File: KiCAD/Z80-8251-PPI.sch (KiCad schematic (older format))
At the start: 31 parts, among them J1 SBC8080 BUS, J2 8251-CE, J3 PPI-CE, J4 232C-CON, J5 CON-A, J6 CON-B, J7 OPM-CE, P1 Power, P2 Analog, P3 Digital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

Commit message: REV2 回路図、製造データ出力
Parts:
- removed J2: 8251-CE, Pin_Headers:Pin_Header_Straight_2x08, symbol Z80-8251-PPI-rescue:Conn_02x08_Odd_Even
- removed J3: PPI-CE, Pin_Headers:Pin_Header_Straight_2x08, symbol Z80-8251-PPI-rescue:Conn_02x08_Odd_Even
- removed J7: OPM-CE, Pin_Headers:Pin_Header_Straight_2x08, symbol Z80-8251-PPI-rescue:Conn_02x08_Odd_Even
- removed P1: Power, Socket_Arduino_Uno:Socket_Strip_Arduino_1x08, symbol Z80-8251-PPI-rescue:CONN_01X08
- removed P2: Analog, Socket_Arduino_Uno:Socket_Strip_Arduino_1x06, symbol Z80-8251-PPI-rescue:CONN_01X06
- removed P3: Digital, Socket_Arduino_Uno:Socket_Strip_Arduino_1x10, symbol Z80-8251-PPI-rescue:CONN_01X10
- removed P4: Digital, Socket_Arduino_Uno:Socket_Strip_Arduino_1x08, symbol Z80-8251-PPI-rescue:CONN_01X08
- removed P5, P6, P7, P8: CONN_01X01, Socket_Arduino_Uno:Arduino_1pin, symbol Z80-8251-PPI-rescue:CONN_01X01
- removed R2: 100k, Resistor_THT:R_Axial_DIN0207_L6.3mm_D2.5mm_P10.16mm_Horizontal, symbol Device:R
- removed R3: 1k, Resistor_THT:R_Axial_DIN0207_L6.3mm_D2.5mm_P10.16mm_Horizontal, symbol Device:R
- removed U1: 74HC138, Housings_DIP:DIP-16_W7.62mm_Socket, symbol Z80-8251-PPI-rescue:74LS138
- added C8, C9: 0.1u, Capacitor_THT:C_Rect_L4.0mm_W2.5mm_P2.50mm, symbol Z80-8251-PPI-rescue:C
- added J2: ADDR_JP, Connector_PinHeader_2.54mm:PinHeader_2x04_P2.54mm_Vertical, symbol Connector_Generic:Conn_02x04_Odd_Even
- added J3: IR JP, Connector_PinHeader_2.54mm:PinHeader_1x05_P2.54mm_Horizontal, symbol Connector_Generic:Conn_01x05
- added J7: SERIAL JP, Connector_PinHeader_2.54mm:PinHeader_2x04_P2.54mm_Vertical, symbol Connector_Generic:Conn_02x04_Odd_Even
- added J8: SP JP, Connector_PinHeader_2.54mm:PinHeader_1x02_P2.54mm_Horizontal, symbol Connector_Generic:Conn_01x02
- added JP1: A7_JP, Connector_PinHeader_2.54mm:PinHeader_1x03_P2.54mm_Vertical, symbol Jumper:Jumper_3_Open
- added JP2: VCC_JP, Connector_PinHeader_2.54mm:PinHeader_1x03_P2.54mm_Vertical, symbol Jumper:Jumper_3_Open
- added MH1, MH2, MH3, MH4: MountingHole, MountingHole:MountingHole_3.2mm_M3, symbol Mechanical:MountingHole
- added R2, R4, R5, R6: 100k, Resistor_THT:R_Axial_DIN0207_L6.3mm_D2.5mm_P10.16mm_Horizontal, symbol Device:R_US
- added R3: 1k, Resistor_THT:R_Axial_DIN0207_L6.3mm_D2.5mm_P10.16mm_Horizontal, symbol Device:R_US
- added U1: 74LS139, Package_DIP:DIP-16_W7.62mm_Socket, symbol 74xx:74LS139
- added U5: 8259, Package_DIP:DIP-28_W15.24mm_Socket, symbol Interface:8259
- added U6: 8254, Package_DIP:DIP-24_W15.24mm_Socket, symbol Timer:8254
- C1, C2, C3, C4, C5, C6: footprint Capacitors_THT:C_Rect_L4.0mm_W2.5mm_P2.50mm -> Capacitor_THT:C_Rect_L4.0mm_W2.5mm_P2.50mm
- J4: footprint Pin_Headers:Pin_Header_Angled_1x06 -> Connector_PinHeader_2.54mm:PinHeader_1x06_P2.54mm_Horizontal
- J5, J6: footprint Pin_Headers:Pin_Header_Straight_2x07_Pitch2.54mm -> Connector_PinHeader_2.54mm:PinHeader_2x07_P2.54mm_Vertical
- R1: footprint Resistors_THT:R_Axial_DIN0207_L6.3mm_D2.5mm_P10.16mm_Horizontal -> Resistor_THT:R_Axial_DIN0207_L6.3mm_D2.5mm_P10.16mm_Horizontal
- U2: footprint Housings_DIP:DIP-28_W15.24mm_Socket -> Package_DIP:DIP-28_W15.24mm_Socket
- U3: footprint Housings_DIP:DIP-40_W15.24mm -> Package_DIP:DIP-40_W15.24mm_Socket
- Y1: value 4.9152MHz -> 19.6608MHz
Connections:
- net labels added: 8251-A, 8251A-CS, 8254-1, 8254-2, 8254-CS, 8255-CS, 8259-CS, IR, IR0, IR1, IR2, IR3, IR6, SBC5V, ~INTA
- net labels removed: A2, ~CE, ~RESIN
- wire segments 383 -> 332
- no-connect marks 43 -> 28
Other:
- note added: "+5V"
- note added: "1228.8kHz"
- note added: "153.6kHz"
- note added: "307.2kHz"
- note added: "614.4kHz"
- note added: "CTS"
- note added: "GND"
- note added: "RTS"
- note added: "RxD"
- note added: "TxD"
- note removed: "1"
- note removed: "Holes"
- note removed: "Shield for Arduino that uses\nthe same pin disposition\nlike "Uno" board Rev 3."
- moved on the sheet: C1, C2, C3, C4, C5, C6, C7, J1, J5, J6, R1, U4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

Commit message: REV3 回路図、パターン検討 その1
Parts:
- removed JP2: VCC_JP, Connector_PinHeader_2.54mm:PinHeader_1x03_P2.54mm_Vertical, symbol Jumper:Jumper_3_Open
- added C10: 22p, Capacitor_THT:C_Disc_D3.0mm_W1.6mm_P2.50mm, symbol Device:C_Small
- added JP2: USB POWER, Jumper:SolderJumper-2_P1.3mm_Open_RoundedPad1.0x1.5mm, symbol Jumper:SolderJumper_2_Open
- added JP3: G0 JP, Jumper:SolderJumper-2_P1.3mm_Open_RoundedPad1.0x1.5mm, symbol Jumper:SolderJumper_2_Open
- added JP4: G1 JP, Jumper:SolderJumper-2_P1.3mm_Open_RoundedPad1.0x1.5mm, symbol Jumper:SolderJumper_2_Open
- added JP5: G2 JP, Jumper:SolderJumper-2_P1.3mm_Open_RoundedPad1.0x1.5mm, symbol Jumper:SolderJumper_2_Open
- added JP6, JP7: 8254-1JP, Jumper:SolderJumper-3_P1.3mm_Bridged12_RoundedPad1.0x1.5mm, symbol Jumper:SolderJumper_3_Bridged12
- C1, C2, C3, C4, C5, C6, C8, C9: footprint Capacitor_THT:C_Rect_L4.0mm_W2.5mm_P2.50mm -> Capacitor_THT:C_Disc_D3.0mm_W1.6mm_P2.50mm
- U5: symbol Interface:8259 -> Z80-8251-PPI-rescue:8259-Interface
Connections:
- net labels added: G0, G1, G2
- net labels removed: SBC5V
- wire segments 332 -> 359
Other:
- moved on the sheet: J8, R2

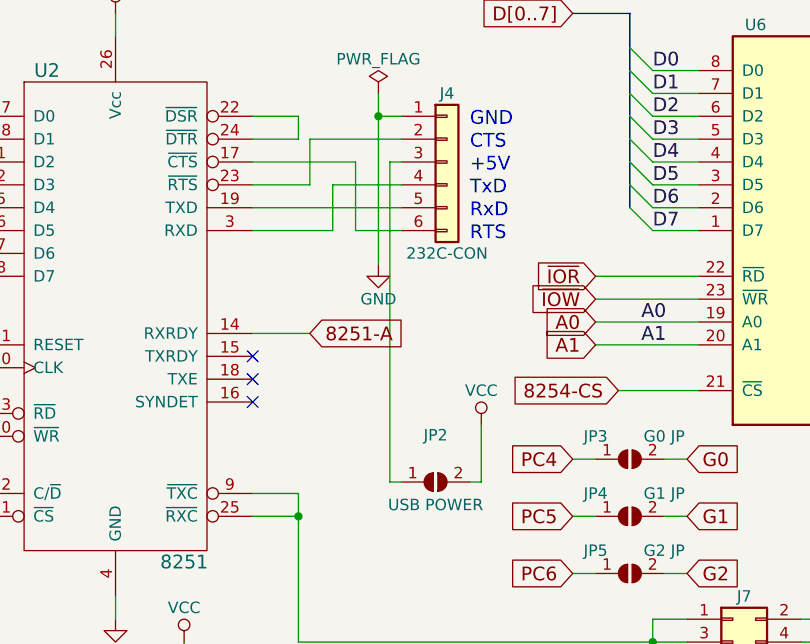
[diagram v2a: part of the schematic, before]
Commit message: FTDI +5Vへダイオード追加
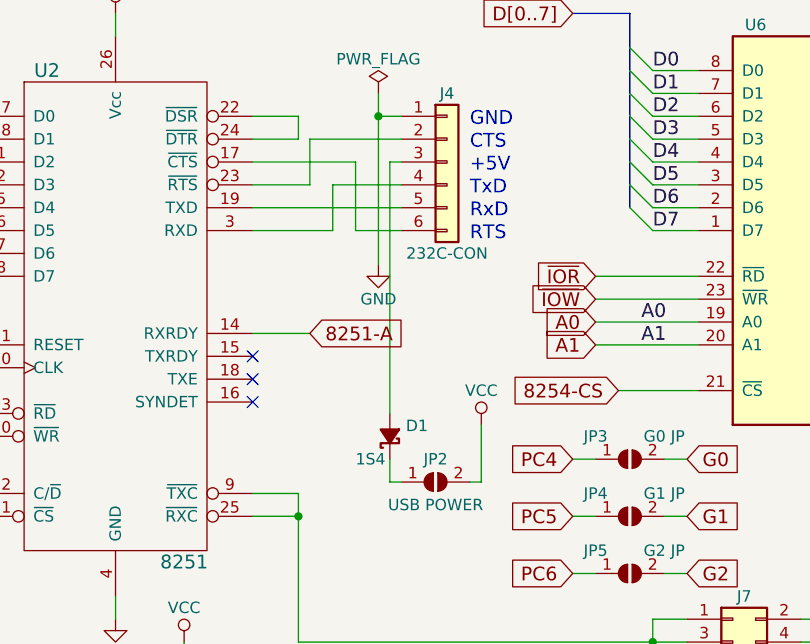
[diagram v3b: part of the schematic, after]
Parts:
- added D1: 1S4, Diode_THT:D_DO-34_SOD68_P7.62mm_Horizontal, symbol Device:D_Schottky_Small_ALT
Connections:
- net at J4.3 (Pin_3): now also D1.2 (A); no longer JP2.1 (A)
- new net: D1.1 (K), JP2.1 (A)
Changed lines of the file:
@@
 Wire Wire Line
 	6700 1450 6650 1450
-Wire Wire Line
-	6650 1450 6650 2850
 $Comp
 L Z80-8251-PPI-rescue:C C8
@@
 U 1 1 5F58D8D7
 P 6850 2850
-F 0 "JP2" H 6850 3055 50  0000 C CNN
+F 0 "JP2" H 6850 2950 50  0000 C CNN
 F 1 "USB POWER" H 6850 2750 50  0000 C CNN
 F 2 "Jumper:SolderJumper-2_P1.3mm_Open_RoundedPad1.0x1.5mm" H 6850 2850 50  0001 C CNN
@@
 Wire Wire Line
 	10200 1850 9200 1850
+$Comp
+L Device:D_Schottky_Small_ALT D1
+U 1 1 5FB0676C
+P 6650 2650
+F 0 "D1" V 6696 2580 50  0000 R CNN
+F 1 "1S4" V 6550 2800 50  0000 R CNN
+F 2 "Diode_THT:D_DO-34_SOD68_P7.62mm_Horizontal" V 6650 2650 50  0001 C CNN
+F 3 "~" V 6650 2650 50  0001 C CNN
+	1    6650 2650
+	0    -1   -1   0
+$EndComp
+Wire Wire Line
+	6650 1450 6650 2550
+Wire Wire Line
+	6650 2750 6650 2850
 Wire Bus Line
 	3850 4900 3850 5050
